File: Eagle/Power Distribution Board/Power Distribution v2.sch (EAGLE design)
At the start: 43 parts, among them IC1 INA138, IC2 INA138, IC3 INA138

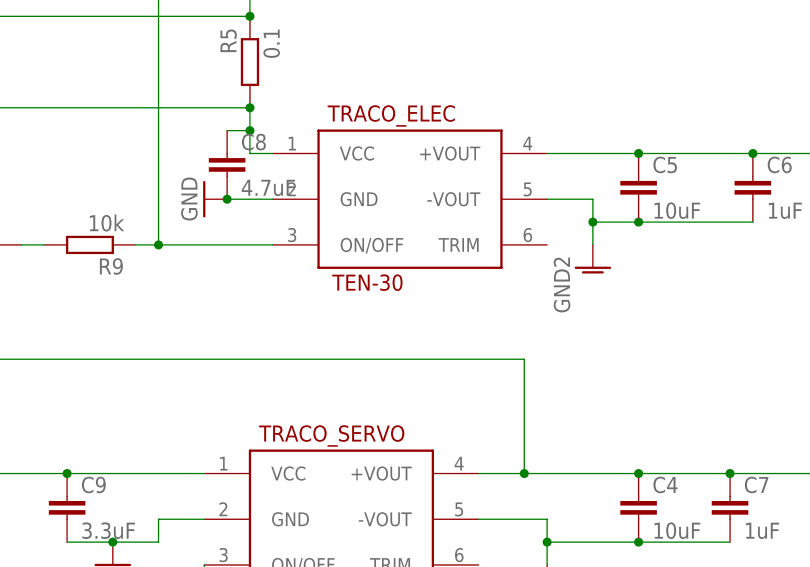
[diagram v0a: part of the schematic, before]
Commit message: Reorganise projects & cleanup
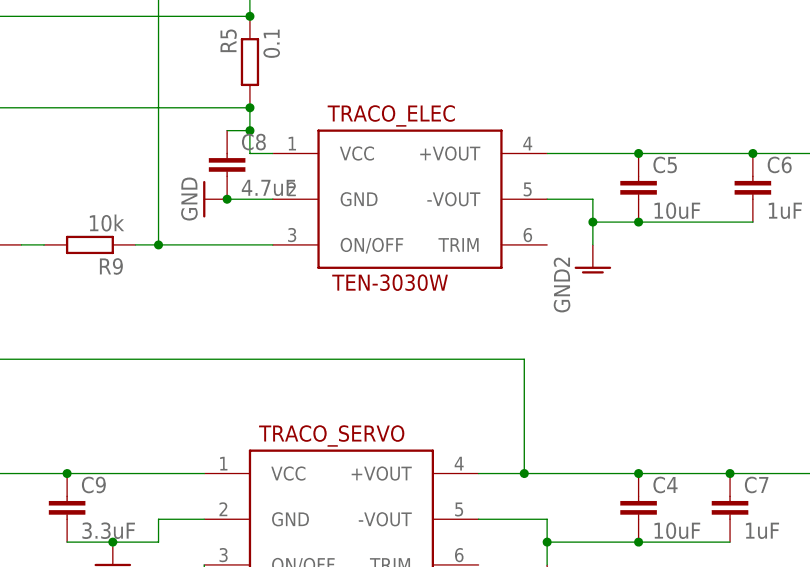
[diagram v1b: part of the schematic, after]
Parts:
- TRACO_ELEC: value TEN-30 -> TEN-3030W; device custom:TEN-30 -> custom:TEN-3030W
- TRACO_SERVO: device custom:TEN-30 -> custom:TEN-3050W
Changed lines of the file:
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@@
 <part name="GND12" library="supply1" deviceset="GND" device=""/>
 <part name="GND15" library="supply1" deviceset="GND" device=""/>
-<part name="TRACO_ELEC" library="custom" deviceset="TEN-30" device=""/>
-<part name="TRACO_SERVO" library="custom" deviceset="TEN-30" device="" value="TEN-50"/>
+<part name="TRACO_ELEC" library="custom" deviceset="TEN-30" device="30W"/>
+<part name="TRACO_SERVO" library="custom" deviceset="TEN-30" device="50W" value="TEN-50"/>
 <part name="OUT_12V_SERVO" library="con-phoenix-508" deviceset="MSTBA2" device=""/>
 <part name="C4" library="rcl" deviceset="C-EU" device="C1812" value="10uF"/>
